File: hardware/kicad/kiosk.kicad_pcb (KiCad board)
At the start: 2 copper layers, 170 x 116 mm, 15 parts, among them J10 TerminalBlock_MaiXu_MX126-5.0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, J11 TerminalBlock_MaiXu_MX126-5.0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, J13 PinHeader_1x09_P2.54mm_Vertic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, J3 PinSocket_1x14_P2.54mm_Vertic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, J4 PinSocket_1x06_P2.54mm_Vertic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, J5 PinSocket_1x04_P2.54mm_Vertic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, J6 PinSocket_1x06_P2.54mm_Vertic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, J7 PinSocket_1x07_P2.54mm_Vertic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, J9 PinHeader_1x03_P2.54mm_Vertic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, U1 ESP32-S3-CAM

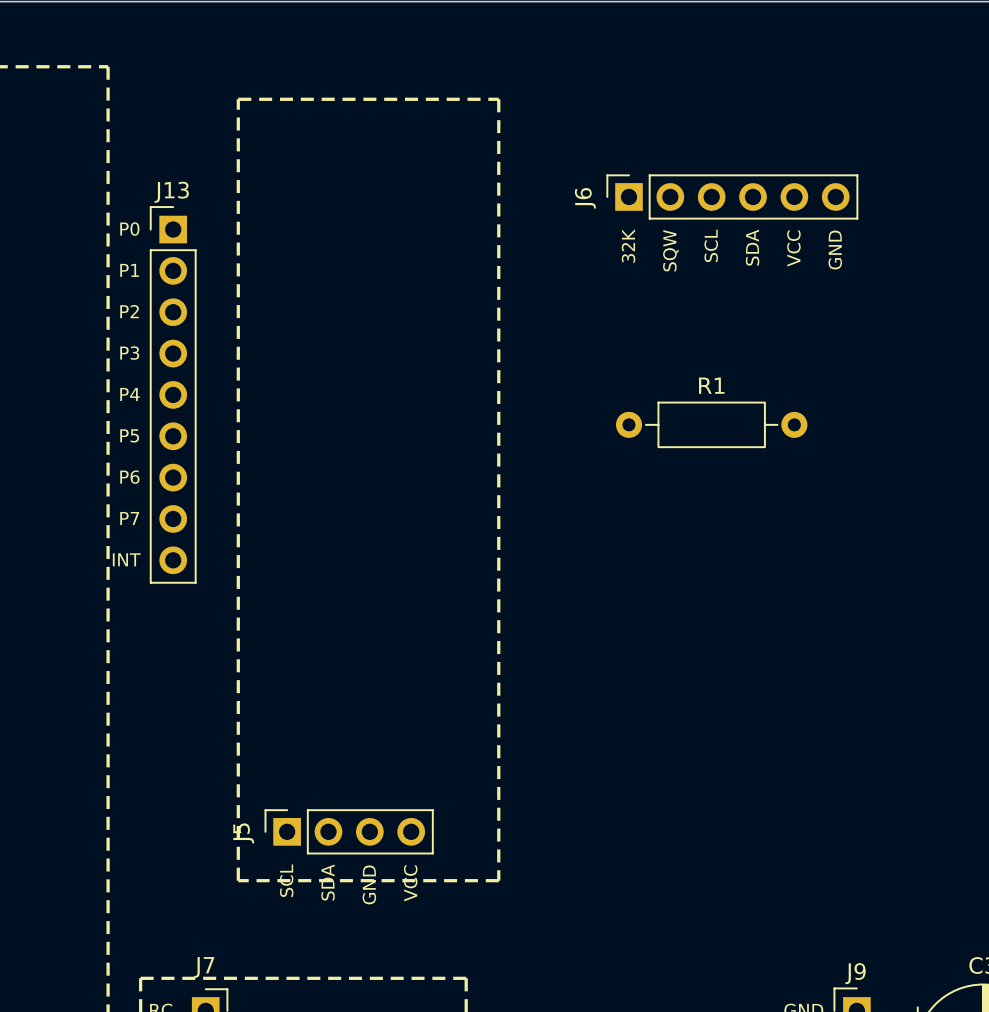
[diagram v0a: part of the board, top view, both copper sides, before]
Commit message: fix(hardware): turn the expander round
Its bus row moves to the top edge of the outline, its port row to the
right side, and the four socket pins reverse - which is what a half turn
does to all three at once.

The socket is rotated rather than rewired: at 270 degrees instead of 90,
the pin numbers follow the turn and the nets stay on the pins they were
always on. Editing the net order by hand is how the amplifier ended up
mirrored two commits ago.

J13 crosses to the far side with it, 5 mm clear of the outline and 9 mm
from the RTC, so a soldering iron still reaches the holes.
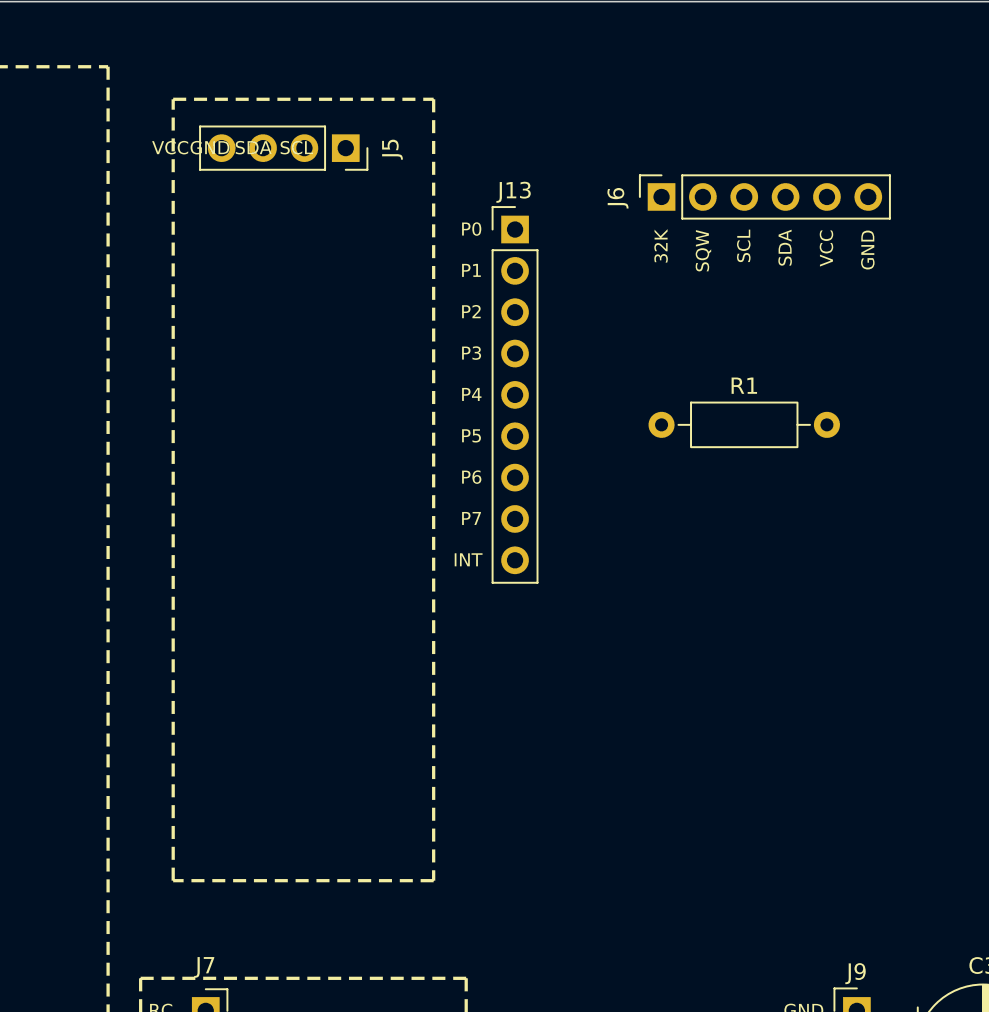
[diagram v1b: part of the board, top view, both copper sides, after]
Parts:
- moved J5 42.2 mm to (118.6, 9.00), turned to -90 degrees
- moved J13 21.0 mm to (129.0, 14.0)
- moved J6 2.00 mm to (138.0, 12.0)
- moved R1 2.00 mm to (138.0, 26.0)

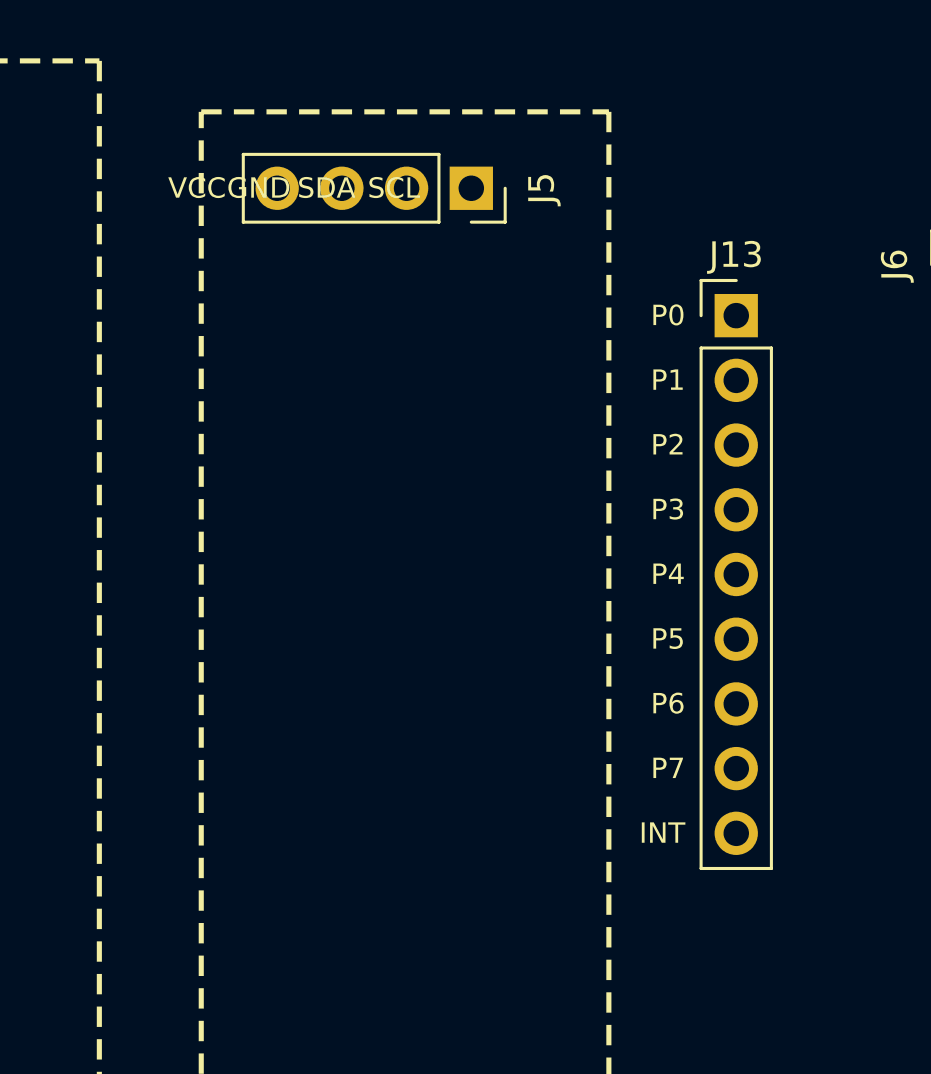
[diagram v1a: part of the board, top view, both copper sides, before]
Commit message: fix(hardware): reverse both expander rows so INT lands beside VCC
The bus row reads SCL SDA GND VCC left to right and the port row runs INT
at the top down to P0, which puts INT and VCC 11.5 mm apart at the same
corner - the arrangement the part actually has.

Both done by turning the footprint, J5 back to 90 degrees and J13 to 180,
so the pin numbers travel with the rotation. The nets were never touched:
they sit on the pins they have always sat on, and the pins moved.
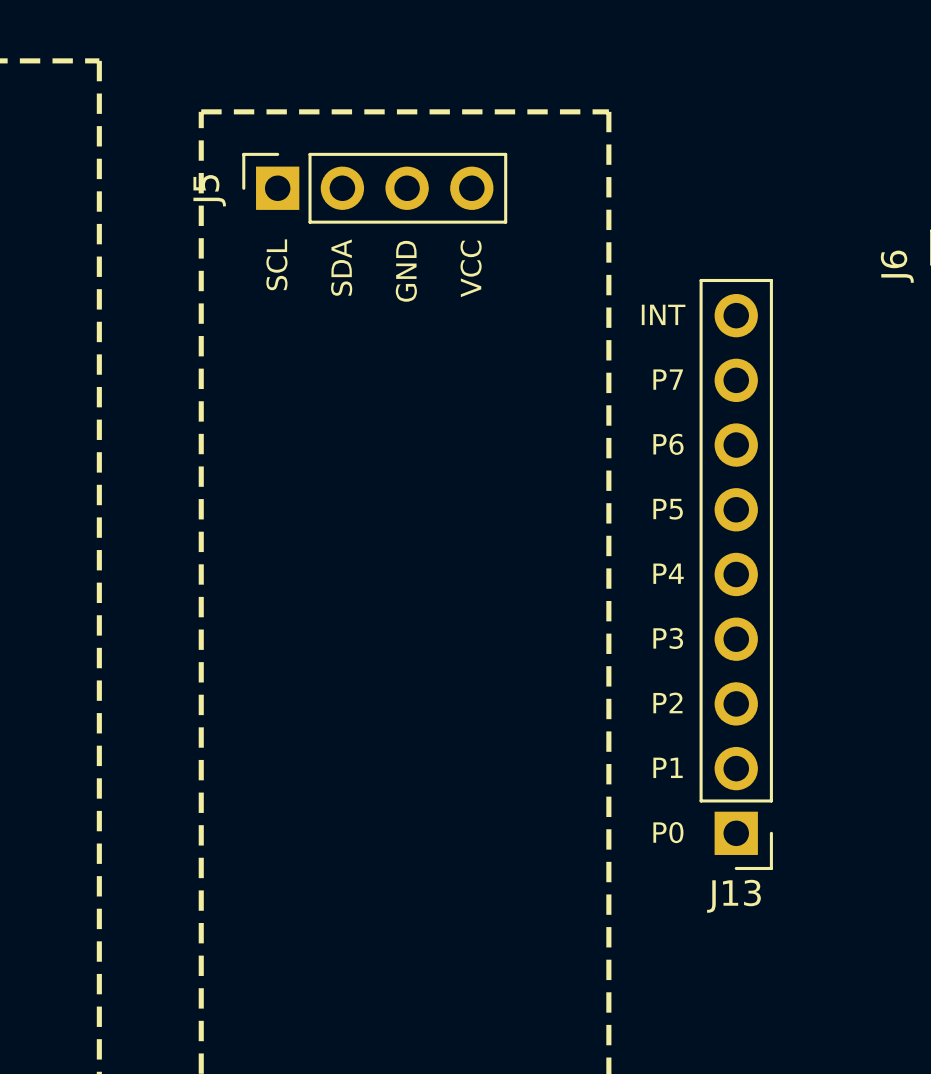
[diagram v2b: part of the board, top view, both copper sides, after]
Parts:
- moved J13 20.3 mm to (129.0, 34.3), turned to 180 degrees
- moved J5 7.60 mm to (111.0, 9.00), turned to 90 degrees
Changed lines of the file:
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@@
 	(footprint "Connector_PinSocket_2.54mm:PinSocket_1x04_P2.54mm_Vertical"
 		(layer "F.Cu")
-		(at 118.6 9 -90)
+		(at 111 9 90)
 		(descr "Through hole straight socket strip, 1x04, 2.54mm pitch, single row (from Kicad 4.0.7), script generated")
 		(tags "Through hole socket strip THT 1x04 2.54mm single row")
 		(property "Reference" "J5"
-			(at 0 -2.77 270)
+			(at 0 -2.77 90)
 			(layer "F.SilkS")
 			(effects
@@
 		)
 		(property "Value" "PinSocket_1x04_P2.54mm_Vertical"
-			(at 0 10.39 270)
+			(at 0 10.39 90)
 			(layer "F.Fab")
 			(effects
@@
 		)
 		(property "Datasheet" ""
-			(at 0 0 270)
+			(at 0 0 90)
 			(layer "F.Fab")
 			(hide yes)
@@
 		)
 		(property "Description" ""
-			(at 0 0 270)
+			(at 0 0 90)
 			(layer "F.Fab")
 			(hide yes)
@@
 		)
 		(property "KiLib_Generator" "connector/pin_header_socket"
-			(at 0 0 270)
+			(at 0 0 90)
 			(layer "F.SilkS")
 			(hide yes)
@@
 		(duplicate_pad_numbers_are_jumpers no)
 		(fp_line
-			(start -1.33 8.95)
-			(end 1.33 8.95)
+			(start 1.33 -1.33)
+			(end 1.33 0)
 			(stroke
 				(width 0.12)
@@
 		)
 		(fp_line
-			(start -1.33 1.27)
-			(end -1.33 8.95)
+			(start 0 -1.33)
+			(end 1.33 -1.33)
 			(stroke
 				(width 0.12)
@@
 		)
 		(fp_line
-			(start -1.33 1.27)
-			(end 1.33 1.27)
+			(start 1.33 1.27)
+			(end 1.33 8.95)
 			(stroke
 				(width 0.12)
@@
 		)
 		(fp_line
-			(start 1.33 1.27)
-			(end 1.33 8.95)
+			(start -1.33 1.27)
+			(end 1.33 1.27)
 			(stroke
 				(width 0.12)
@@
 		)
 		(fp_line
-			(start 0 -1.33)
-			(end 1.33 -1.33)
+			(start -1.33 1.27)
+			(end -1.33 8.95)
 			(stroke
 				(width 0.12)
@@
 		)
 		(fp_line
-			(start 1.33 -1.33)
-			(end 1.33 0)
+			(start -1.33 8.95)
+			(end 1.33 8.95)
 			(stroke
 				(width 0.12)
@@
 		)
 		(fp_line
-			(start -1.77 9.39)
-			(end -1.77 -1.77)
+			(start 1.77 -1.77)
+			(end 1.77 9.39)
 			(stroke
 				(width 0.05)
@@
 		)
 		(fp_line
-			(start 1.77 9.39)
-			(end -1.77 9.39)
+			(start -1.77 -1.77)
+			(end 1.77 -1.77)
 			(stroke
 				(width 0.05)
@@
 		)
 		(fp_line
-			(start -1.77 -1.77)
-			(end 1.77 -1.77)
+			(start 1.77 9.39)
+			(end -1.77 9.39)
 			(stroke
 				(width 0.05)
@@
 		)
 		(fp_line
-			(start 1.77 -1.77)
-			(end 1.77 9.39)
+			(start -1.77 9.39)
+			(end -1.77 -1.77)
 			(stroke
 				(width 0.05)
@@
 		)
 		(fp_line
-			(start -1.27 8.89)
-			(end -1.27 -1.27)
+			(start 0.635 -1.27)
+			(end 1.27 -0.635)
 			(stroke
 				(width 0.1)
@@
 		)
 		(fp_line
-			(start 1.27 8.89)
-			(end -1.27 8.89)
+			(start -1.27 -1.27)
+			(end 0.635 -1.27)
 			(stroke
 				(width 0.1)
@@
 		)
 		(fp_line
-			(start -1.27 -1.27)
-			(end 0.635 -1.27)
+			(start 1.27 8.89)
+			(end -1.27 8.89)
 			(stroke
 				(width 0.1)
@@
 		)
 		(fp_line
-			(start 0.635 -1.27)
-			(end 1.27 -0.635)
+			(start -1.27 8.89)
+			(end -1.27 -1.27)
 			(stroke
 				(width 0.1)
@@
 	(footprint "Connector_PinHeader_2.54mm:PinHeader_1x09_P2.54mm_Vertical"
 		(layer "F.Cu")
-		(at 129 14)
+		(at 129 34.32 180)
 		(descr "Through hole straight pin header, 1x09, 2.54mm pitch, single row")
 		(tags "Through hole pin header THT 1x09 2.54mm single row")
 		(property "Reference" "J13"
-			(at 0 -2.38 0)
+			(at 0 -2.38 180)
 			(layer "F.SilkS")
 			(effects
@@
 		)
 		(property "Value" "PinHeader_1x09_P2.54mm_Vertical"
-			(at 0 22.7 0)
+			(at 0 22.7 180)
 			(layer "F.Fab")
 			(effects
@@
 		)
 		(property "Datasheet" ""
-			(at 0 0 0)
+			(at 0 0 180)
 			(layer "F.Fab")
 			(hide yes)
@@
 		)
 		(property "Description" ""
-			(at 0 0 0)
+			(at 0 0 180)
 			(layer "F.Fab")
 			(hide yes)
@@
 		)
 		(property "KiLib_Generator" "connector/pin_header_socket"
-			(at 0 0 0)
+			(at 0 0 180)
 			(layer "F.SilkS")
 			(hide yes)
@@
 		(duplicate_pad_numbers_are_jumpers no)
 		(fp_line
-			(start -1.38 -1.38)
-			(end 0 -1.38)
+			(start 1.38 1.27)
+			(end 1.38 21.7)
 			(stroke
 				(width 0.12)
@@
 		)
 		(fp_line
-			(start -1.38 0)
-			(end -1.38 -1.38)
+			(start -1.38 21.7)
+			(end 1.38 21.7)
 			(stroke
 				(width 0.12)
@@
 		(fp_line
 			(start -1.38 1.27)
-			(end -1.38 21.7)
+			(end 1.38 1.27)
 			(stroke
 				(width 0.12)
@@
 		(fp_line
 			(start -1.38 1.27)
-			(end 1.38 1.27)
+			(end -1.38 21.7)
 			(stroke
 				(width 0.12)
@@
 		)
 		(fp_line
-			(start -1.38 21.7)
-			(end 1.38 21.7)
+			(start -1.38 0)
+			(end -1.38 -1.38)
 			(stroke
 				(width 0.12)
@@
 		)
 		(fp_line
-			(start 1.38 1.27)
-			(end 1.38 21.7)
+			(start -1.38 -1.38)
+			(end 0 -1.38)
 			(stroke
 				(width 0.12)
@@
 		)
 		(fp_line
-			(start -1.27 -0.635)
-			(end -0.635 -1.27)
+			(start 1.27 21.59)
+			(end -1.27 21.59)
 			(stroke
 				(width 0.1)
@@
 		)
 		(fp_line
-			(start -1.27 21.59)
-			(end -1.27 -0.635)
+			(start 1.27 -1.27)
+			(end 1.27 21.59)
 			(stroke
 				(width 0.1)
@@
 		)
 		(fp_line
-			(start 1.27 -1.27)
-			(end 1.27 21.59)
+			(start -1.27 21.59)
+			(end -1.27 -0.635)
 			(stroke
 				(width 0.1)
@@
 		)
 		(fp_line
-			(start 1.27 21.59)
-			(end -1.27 21.59)
+			(start -1.27 -0.635)
+			(end -0.635 -1.27)
 			(stroke
 				(width 0.1)
@@
 		)
 	)
-	(gr_text "VCC"
-		(at 108.98 9 0)
-		(layer "F.SilkS")
-		(effects
-			(font
-				(size 0.8 0.8)
-				(thickness 0.12)
-			)
-			(justify right)
-		)
-	)
-	(gr_text "GND"
-		(at 111.52 9 0)
-		(layer "F.SilkS")
-		(effects
-			(font
-				(size 0.8 0.8)
-				(thickness 0.12)
-			)
-			(justify right)
-		)
-	)
-	(gr_text "SDA"
-		(at 114.06 9 0)
-		(layer "F.SilkS")
-		(effects
-			(font
-				(size 0.8 0.8)
-				(thickness 0.12)
-			)
-			(justify right)
-		)
-	)
-	(gr_text "SCL"
-		(at 116.6 9 0)
-		(layer "F.SilkS")
-		(effects
-			(font
-				(size 0.8 0.8)
-				(thickness 0.12)
-			)
-			(justify right)
-		)
-	)
-	(gr_text "P0"
+	(gr_text "INT"
 		(at 127 14 0)
 		(layer "F.SilkS")
@@
 		)
 	)
-	(gr_text "P1"
+	(gr_text "P7"
 		(at 127 16.54 0)
 		(layer "F.SilkS")
@@
 		)
 	)
-	(gr_text "P2"
+	(gr_text "P6"
 		(at 127 19.08 0)
 		(layer "F.SilkS")
@@
 		)
 	)
-	(gr_text "P3"
+	(gr_text "P5"
 		(at 127 21.62 0)
 		(layer "F.SilkS")
@@
 		)
 	)
-	(gr_text "P5"
+	(gr_text "P3"
 		(at 127 26.7 0)
 		(layer "F.SilkS")
@@
 		)
 	)
-	(gr_text "P6"
+	(gr_text "P2"
 		(at 127 29.24 0)
 		(layer "F.SilkS")
@@
 		)
 	)
-	(gr_text "P7"
+	(gr_text "P1"
 		(at 127 31.78 0)
 		(layer "F.SilkS")
@@
 		)
 	)
-	(gr_text "INT"
+	(gr_text "P0"
 		(at 127 34.32 0)
 		(layer "F.SilkS")
@@
 		(layer "F.SilkS")
 		(effects
+			(font
+				(size 0.8 0.8)
+				(thickness 0.12)
+			)
+			(justify right)
+		)
+	)
+	(gr_text "SCL"
+		(at 111 11 90)
+		(layer "F.SilkS")
+		(effects
+			(font
+				(size 0.8 0.8)
+				(thickness 0.12)
+			)
+			(justify right)
+		)
+	)
+	(gr_text "SDA"
+		(at 113.54 11 90)
+		(layer "F.SilkS")
+		(effects
+			(font
+				(size 0.8 0.8)
+				(thickness 0.12)
+			)
+			(justify right)
+		)
+	)
+	(gr_text "GND"
+		(at 116.08 11 90)
+		(layer "F.SilkS")
+		(effects
+			(font
+				(size 0.8 0.8)
+				(thickness 0.12)
+			)
+			(justify right)
+		)
+	)
+	(gr_text "VCC"
+		(at 118.62 11 90)
+		(layer "F.SilkS")
+		(effects

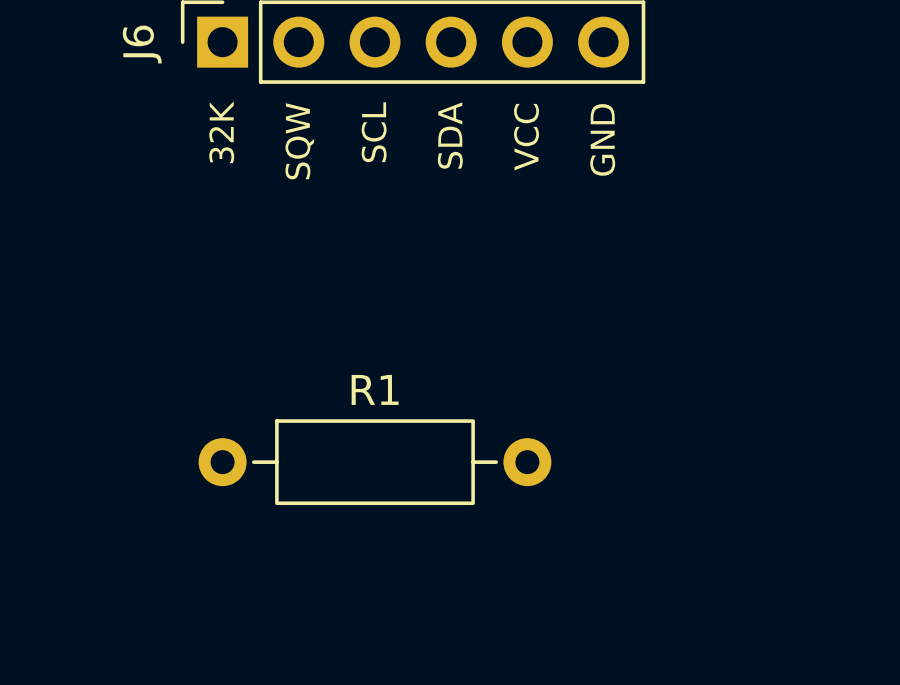
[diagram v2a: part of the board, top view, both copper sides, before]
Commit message: fix(hardware): tighten the pull-up against the RTC header
Both of R1's legs now reach their nets in 8.4 and 9.4 mm, where before it
was 11 and 23. The RTC's header is the one place on this board where 3V3
and SDA sit 2.54 mm apart, so it is where a part needing both lands on
the shortest copper.

Beside the ESP32 would follow the usual habit of putting pull-ups at the
master, and would be worse here: SDA would come down to 7 mm but 3V3
would go out to 32. The bus is a single node either way - rise time is
total capacitance times resistance, and where the resistor sits changes
neither.
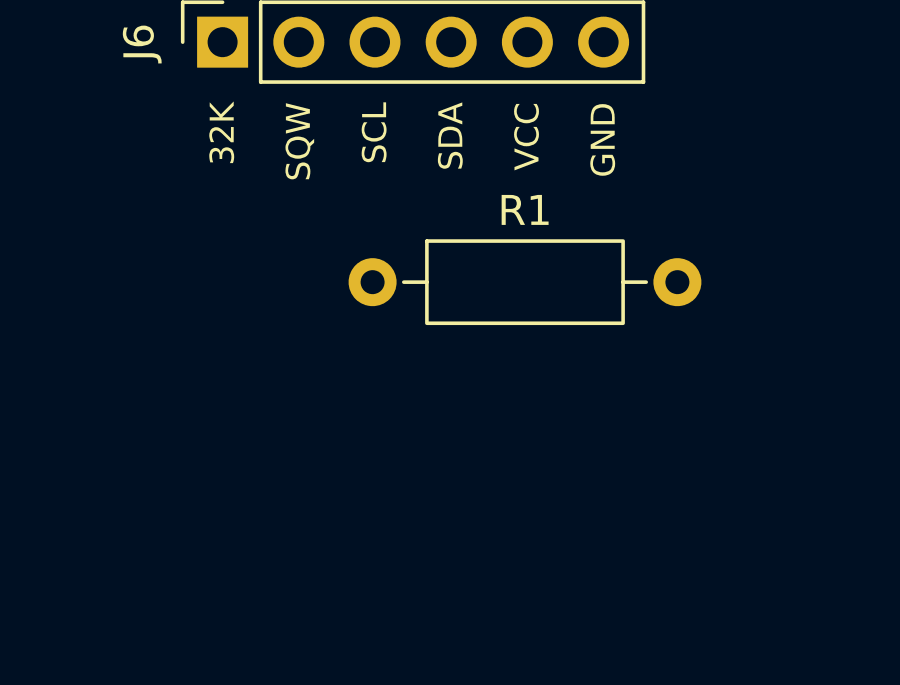
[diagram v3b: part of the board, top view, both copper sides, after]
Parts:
- moved R1 7.81 mm to (143.0, 20.0)
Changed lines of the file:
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@@
 	(footprint "Resistor_THT:R_Axial_DIN0207_L6.3mm_D2.5mm_P10.16mm_Horizontal"
 		(layer "F.Cu")
-		(at 138 26)
+		(at 143 20)
 		(descr "Resistor, Axial_DIN0207 series, Axial, Horizontal, pin pitch=10.16mm, 0.25W = 1/4W, length*diameter=6.3*2.5mm^2, http://cdn-reichelt.de/documents/datenblatt/B400/1_4W%23YAG.pdf")
 		(tags "Resistor Axial_DIN0207 series Axial Horizontal pin pitch 10.16mm 0.25W = 1/4W length 6.3mm diameter 2.5mm")
